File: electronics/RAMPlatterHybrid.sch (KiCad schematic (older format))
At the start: 50 parts, among them J1 Raspberry_Pi_2_3, J2 Raspberry_Pi_2_3, U1 LM358, U2 74LVC74APW, U3 AV2-8.4-10, U4 AV2-8.4-10, U5 HC4046A, U6 CD74HC4059, U7 AP1117-33, U8 WM8750

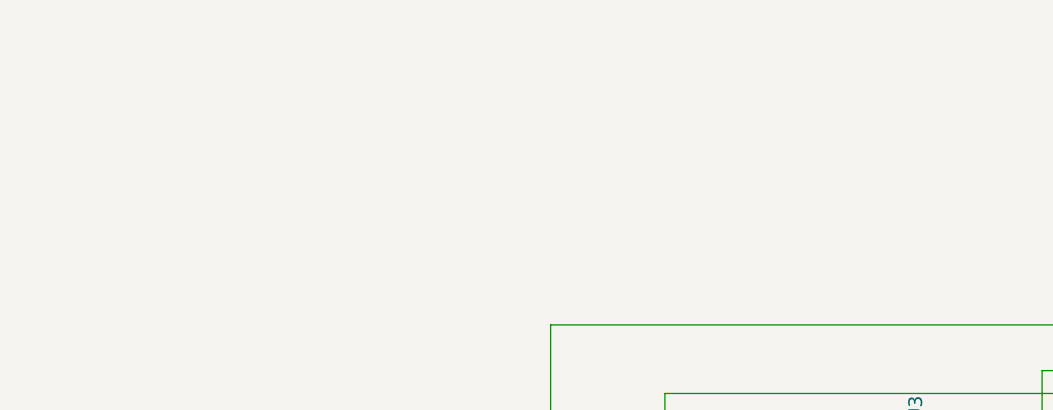
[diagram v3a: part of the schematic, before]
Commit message: added a wiki link to the new required hardware to the sch file.
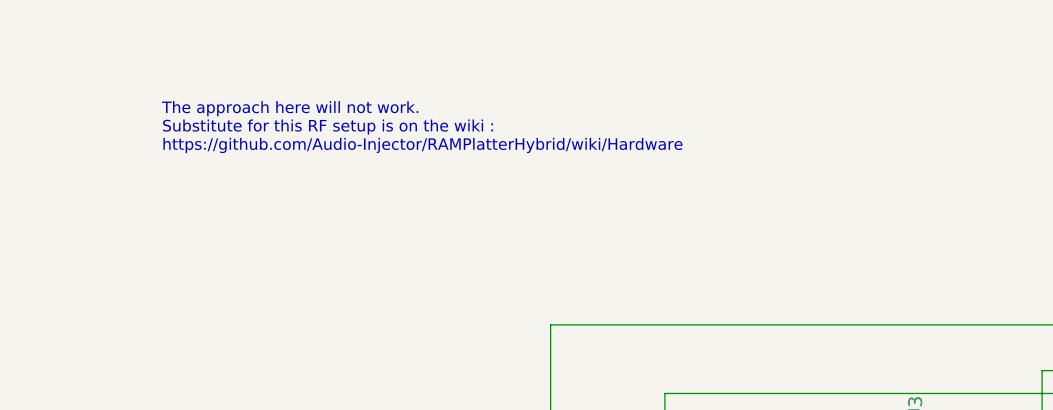
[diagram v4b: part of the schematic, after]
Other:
- note added: "The approach here will not work.\nSubstitute for this RF setup is on the wiki :\nhttps://github.com/Audio-Injector/RAMPlatterHybrid/wiki/Hardware"
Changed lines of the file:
@@
 Wire Wire Line
 	6450 5800 6850 5800
+Text Notes 1400 1150 0    50   ~ 0
+The approach here will not work.\nSubstitute for this RF setup is on the wiki :\nhttps://github.com/Audio-Injector/RAMPlatterHybrid/wiki/Hardware
 $EndSCHEMATC
